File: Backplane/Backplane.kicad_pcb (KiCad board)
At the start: 2 copper layers, 245 parts, among them J3 Bus_PCI_Express_x1, J4 Bus_PCI_Express_x1, J5 Bus_PCI_Express_x1, J6 Bus_PCI_Express_x1, Q1 CJ2302 S2, Q12 CJ2302 S2, Q13 CJ2302 S2, Q14 CJ2302 S2, Q15 CJ2302 S2, Q16 CJ2302 S2, Q17 CJ2302 S2, Q18 CJ2302 S2, Q19 CJ2302 S2, Q2 CJ2302 S2, Q20 CJ2302 S2, Q21 CJ2302 S2, Q22 CJ2302 S2, Q23 CJ2302 S2, Q24 CJ2302 S2, Q25 CJ2302 S2, Q26 CJ2302 S2, Q27 CJ2302 S2, Q28 CJ2302 S2, Q3 TPHR8504PL,LQ(M1W, Q4 TPHR8504PL,LQ(M1W, Q5 TPHR8504PL,LQ(M1W, Q6 TPHR8504PL,LQ(M1W, Q7 CJ2302 S2, U1 XT60PW-F_C428722, U10 XT60PW-F_C428722, U11 PCA9555PW,118, U12 LM393, U13 LM358, U14 TCA9548APWR, U15 MCP4725A0T-E/CH, U16 MCP4725A0T-E/CH, U2 XT60PW-F_C428722, U22 ADS1115IDGSR, U24 ADS1115IDGSR, U3 LM393, U31 PCA9555PW,118, U32 TCA9548APWR, U33 LM393, U34 UCC27324DR, U35 LM358, U36 MCP4725A0T-E/CH, U37 MCP4725A0T-E/CH, U38 ADS1115IDGSR, U39 ADS1115IDGSR, U4 LM358, U5 TPS54360BDDAR, U6 TPS54360BDDAR, U7 TPS54360BDDAR, U8 UCC27324DR, U9 XT60PW-F_C428722

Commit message: Finished board layout.
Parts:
- moved J3 353.0 mm to (88.5, 203.2)
- moved R24 307.8 mm to (670.1, 97.5)
- moved R25 307.8 mm to (670.1, 100.7)
- moved R26 307.8 mm to (670.1, 104.0)
- moved R27 307.8 mm to (670.1, 107.3)
- moved R28 307.8 mm to (670.1, 110.6)
- moved U12 307.8 mm to (670.8, 91.7)
- moved U13 307.8 mm to (677.1, 91.7)
- moved U3 307.8 mm to (658.3, 91.7)
- moved U4 307.8 mm to (664.6, 91.7)
- moved Q3 307.8 mm to (677.1, 100.7)
- moved Q4 307.8 mm to (684.5, 100.7)
- moved R16 307.8 mm to (664.1, 97.5)
- moved R17 307.8 mm to (664.1, 100.7)
- moved R18 307.8 mm to (664.1, 104.0)
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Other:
- board outline added: 520 x 80 mm

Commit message: All parts are correct.
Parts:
- removed C10, C11, C12, C13, C14, C15, C16, C4, C5: 100n, Resistor_SMD:R_1206_3216Metric_Pad1.30x1.75mm_HandSolder
- removed D32, D33, D34, D35: S5BBF, COMPONENTS:SMBF_L4.3-W3.6-LS5.3-RD
- removed L4: FXL1040-8R2-M, COMPONENTS:IND-SMD_L11.5-W10.0_FXL1040
- removed Q16, Q17, Q23, Q24: CJ2302 S2, COMPONENTS:SOT-23-3_L3.0-W1.7-P0.95-LS2.9-BR
- removed R34, R35, R36, R37, R39, R40, R41, R42, R43, R44, R45, R46, R47, R69, R70, R71, R72, R73, R74, R75, R76, R77, R78, R79, R80, R81, R82: 1k, Resistor_SMD:R_1206_3216Metric_Pad1.30x1.75mm_HandSolder
- removed R38: 8k, Resistor_SMD:R_1206_3216Metric_Pad1.30x1.75mm_HandSolder
- removed U11, U31: PCA9555PW,118, COMPONENTS:TSSOP-24_L7.8-W4.4-P0.65-LS6.4-BL
- removed U12, U3: LM393, COMPONENTS:SOP-8_L4.9-W3.9-P1.27-LS6.0-BL
- removed U13, U4: LM358, COMPONENTS:SOP-8_L4.9-W3.9-P1.27-LS6.0-BL
- removed U14: TCA9548APWR, COMPONENTS:TSSOP-24_L7.8-W4.4-P0.65-LS6.4-BL
- removed U24: ADS1115IDGSR, COMPONENTS:MSOP-10_L3.0-W3.0-P0.50-LS5.0-BL
- removed U36, U37: MCP4725A0T-E/CH, COMPONENTS:SOT-23-6_L2.9-W1.6-P0.95-LS2.8-BL
- removed U5, U6: TPS54360BDDAR, COMPONENTS:SOIC-8_L5.0-W4.0-P1.27-LS6.0-BL-EP2.0
- added C49: 100n, Resistor_SMD:R_1206_3216Metric_Pad1.30x1.75mm_HandSolder, F.Cu at (292.4, 207.6)
- added C50: 100n, Resistor_SMD:R_1206_3216Metric_Pad1.30x1.75mm_HandSolder, F.Cu at (298.3, 191.1)
- added C51: 100n, Resistor_SMD:R_1206_3216Metric_Pad1.30x1.75mm_HandSolder, F.Cu at (298.3, 194.4)
- added C52: 100n, Resistor_SMD:R_1206_3216Metric_Pad1.30x1.75mm_HandSolder, F.Cu at (-106.7, 527.5)
- added C53: 100n, Resistor_SMD:R_1206_3216Metric_Pad1.30x1.75mm_HandSolder, F.Cu at (-106.7, 530.8)
- added C54: 100n, Resistor_SMD:R_1206_3216Metric_Pad1.30x1.75mm_HandSolder, F.Cu at (-106.7, 534.0)
- added C55: 100n, Resistor_SMD:R_1206_3216Metric_Pad1.30x1.75mm_HandSolder, F.Cu at (-106.7, 537.3)
- added C56: 100n, Resistor_SMD:R_1206_3216Metric_Pad1.30x1.75mm_HandSolder, F.Cu at (-106.7, 540.6)
- added C57: 100n, Resistor_SMD:R_1206_3216Metric_Pad1.30x1.75mm_HandSolder, F.Cu at (-106.7, 543.9)
- added C58: 100n, Resistor_SMD:R_1206_3216Metric_Pad1.30x1.75mm_HandSolder, F.Cu at (-106.7, 547.2)
- added C59: 100n, Resistor_SMD:R_1206_3216Metric_Pad1.30x1.75mm_HandSolder, F.Cu at (-106.4, 464.1)
- added C60: 100n, Resistor_SMD:R_1206_3216Metric_Pad1.30x1.75mm_HandSolder, F.Cu at (-106.4, 467.4)
- added C61: 100n, Resistor_SMD:R_1206_3216Metric_Pad1.30x1.75mm_HandSolder, F.Cu at (-106.4, 470.7)
- added C62: 100n, Resistor_SMD:R_1206_3216Metric_Pad1.30x1.75mm_HandSolder, F.Cu at (-106.4, 474.0)
- added C63: 100n, Resistor_SMD:R_1206_3216Metric_Pad1.30x1.75mm_HandSolder, F.Cu at (-106.4, 477.3)
- added C64: 100n, Resistor_SMD:R_1206_3216Metric_Pad1.30x1.75mm_HandSolder, F.Cu at (-106.4, 480.6)
- added C65: 100n, Resistor_SMD:R_1206_3216Metric_Pad1.30x1.75mm_HandSolder, F.Cu at (-106.4, 483.9)
- added D24: LED, LED_SMD:LED_1206_3216Metric, F.Cu at (657.9, -215.7)
- added D25: LED, LED_SMD:LED_1206_3216Metric, F.Cu at (657.9, -212.3)
- added D26: LED, LED_SMD:LED_1206_3216Metric, F.Cu at (657.9, -208.9)
- added D27: LED, LED_SMD:LED_1206_3216Metric, F.Cu at (657.9, -205.5)
- added H1: MountingHole_Pad, MountingHole:MountingHole_3.2mm_M3_Pad_TopBottom, F.Cu at (45.2, 170.0)
- added H2: MountingHole_Pad, MountingHole:MountingHole_3.2mm_M3_Pad_TopBottom, F.Cu at (545.0, 230.0)
- added H3: MountingHole_Pad, MountingHole:MountingHole_3.2mm_M3_Pad_TopBottom, F.Cu at (545.3, 170.0)
- added H4: MountingHole_Pad, MountingHole:MountingHole_3.2mm_M3_Pad_TopBottom, F.Cu at (355.0, 230.0)
- added H5: MountingHole_Pad, MountingHole:MountingHole_3.2mm_M3_Pad_TopBottom, F.Cu at (229.9, 230.0)
- added H6: MountingHole_Pad, MountingHole:MountingHole_3.2mm_M3_Pad_TopBottom, F.Cu at (45.0, 230.0)
- added H7: MountingHole_Pad, MountingHole:MountingHole_3.2mm_M3_Pad_TopBottom, F.Cu at (355.2, 170.0)
- added H8: MountingHole_Pad, MountingHole:MountingHole_3.2mm_M3_Pad_TopBottom, F.Cu at (230.0, 170.0)
- added L1: FXL1040-8R2-M, COMPONENTS:IND-SMD_L11.5-W10.0_FXL1040, F.Cu at (222.0, 442.7)
- added Q10: CJ2302 S2, COMPONENTS:SOT-23-3_L3.0-W1.7-P0.95-LS2.9-BR, F.Cu at (645.1, -140.5)
- added Q11: CJ2302 S2, COMPONENTS:SOT-23-3_L3.0-W1.7-P0.95-LS2.9-BR, F.Cu at (640.0, -79.9)
- added Q8: CJ2302 S2, COMPONENTS:SOT-23-3_L3.0-W1.7-P0.95-LS2.9-BR, F.Cu at (645.1, -149.0)
- added Q9: CJ2302 S2, COMPONENTS:SOT-23-3_L3.0-W1.7-P0.95-LS2.9-BR, F.Cu at (645.1, -144.7)
- added R113: 0, Resistor_SMD:R_1206_3216Metric_Pad1.30x1.75mm_HandSolder, F.Cu at (410.2, 197.2)
- added R114: 1k, Resistor_SMD:R_1206_3216Metric_Pad1.30x1.75mm_HandSolder, F.Cu at (298.3, 197.7)
- added R115: 1k, Resistor_SMD:R_1206_3216Metric_Pad1.30x1.75mm_HandSolder, F.Cu at (298.3, 201.0)
- added R116: 1k, Resistor_SMD:R_1206_3216Metric_Pad1.30x1.75mm_HandSolder, F.Cu at (298.3, 204.3)
- added R117: 1k, Resistor_SMD:R_1206_3216Metric_Pad1.30x1.75mm_HandSolder, F.Cu at (298.3, 207.6)
- added R118: 1k, Resistor_SMD:R_1206_3216Metric_Pad1.30x1.75mm_HandSolder, F.Cu at (304.3, 191.1)
- added R119: 1k, Resistor_SMD:R_1206_3216Metric_Pad1.30x1.75mm_HandSolder, F.Cu at (304.3, 194.4)
- added R120: 1k, Resistor_SMD:R_1206_3216Metric_Pad1.30x1.75mm_HandSolder, F.Cu at (304.3, 197.7)
- added R121: 1k, Resistor_SMD:R_1206_3216Metric_Pad1.30x1.75mm_HandSolder, F.Cu at (304.3, 201.0)
- added R122: 10k, Resistor_SMD:R_1206_3216Metric_Pad1.30x1.75mm_HandSolder, F.Cu at (-106.7, 550.5)
- added R123: 10k, Resistor_SMD:R_1206_3216Metric_Pad1.30x1.75mm_HandSolder, F.Cu at (-100.7, 527.5)
- added R124: 1k, Resistor_SMD:R_1206_3216Metric_Pad1.30x1.75mm_HandSolder, F.Cu at (-100.7, 530.8)
- added R125: 1k, Resistor_SMD:R_1206_3216Metric_Pad1.30x1.75mm_HandSolder, F.Cu at (-100.7, 534.0)
- added R126: 1k, Resistor_SMD:R_1206_3216Metric_Pad1.30x1.75mm_HandSolder, F.Cu at (-100.7, 537.3)
- added R127: 1k, Resistor_SMD:R_1206_3216Metric_Pad1.30x1.75mm_HandSolder, F.Cu at (-100.7, 540.6)
- added R128: 1k, Resistor_SMD:R_1206_3216Metric_Pad1.30x1.75mm_HandSolder, F.Cu at (-100.7, 543.9)
- added R129: 1k, Resistor_SMD:R_1206_3216Metric_Pad1.30x1.75mm_HandSolder, F.Cu at (-100.7, 547.2)
- added R130: 100k, Resistor_SMD:R_1206_3216Metric_Pad1.30x1.75mm_HandSolder, F.Cu at (-100.7, 550.5)
- added R131: 100k, Resistor_SMD:R_1206_3216Metric_Pad1.30x1.75mm_HandSolder, F.Cu at (-94.8, 527.5)
- added R132: 1k, Resistor_SMD:R_1206_3216Metric_Pad1.30x1.75mm_HandSolder, F.Cu at (-94.8, 530.8)
- added R133: 1k, Resistor_SMD:R_1206_3216Metric_Pad1.30x1.75mm_HandSolder, F.Cu at (-94.8, 534.0)
- added R134: 0.003, Resistor_SMD:R_1206_3216Metric_Pad1.30x1.75mm_HandSolder, F.Cu at (-94.8, 537.3)
- added R135: 0.003, Resistor_SMD:R_1206_3216Metric_Pad1.30x1.75mm_HandSolder, F.Cu at (-94.8, 540.6)
- added R136: 10k, Resistor_SMD:R_1206_3216Metric_Pad1.30x1.75mm_HandSolder, F.Cu at (-106.4, 487.2)
- added R137: 10k, Resistor_SMD:R_1206_3216Metric_Pad1.30x1.75mm_HandSolder, F.Cu at (-100.4, 464.1)
- added R138: 1k, Resistor_SMD:R_1206_3216Metric_Pad1.30x1.75mm_HandSolder, F.Cu at (-100.4, 467.4)
- added R139: 1k, Resistor_SMD:R_1206_3216Metric_Pad1.30x1.75mm_HandSolder, F.Cu at (-100.4, 470.7)
- added R140: 1k, Resistor_SMD:R_1206_3216Metric_Pad1.30x1.75mm_HandSolder, F.Cu at (-100.4, 474.0)
- added R141: 1k, Resistor_SMD:R_1206_3216Metric_Pad1.30x1.75mm_HandSolder, F.Cu at (-100.4, 477.3)
- added R142: 1k, Resistor_SMD:R_1206_3216Metric_Pad1.30x1.75mm_HandSolder, F.Cu at (-100.4, 480.6)
- added R143: 1k, Resistor_SMD:R_1206_3216Metric_Pad1.30x1.75mm_HandSolder, F.Cu at (-100.4, 483.9)
- added R144: 100k, Resistor_SMD:R_1206_3216Metric_Pad1.30x1.75mm_HandSolder, F.Cu at (-100.4, 487.2)
- added R145: 100k, Resistor_SMD:R_1206_3216Metric_Pad1.30x1.75mm_HandSolder, F.Cu at (-94.5, 464.1)
- added R146: 1k, Resistor_SMD:R_1206_3216Metric_Pad1.30x1.75mm_HandSolder, F.Cu at (-94.5, 467.4)
- added R147: 1k, Resistor_SMD:R_1206_3216Metric_Pad1.30x1.75mm_HandSolder, F.Cu at (-94.5, 470.7)
- added R148: 0.003, Resistor_SMD:R_1206_3216Metric_Pad1.30x1.75mm_HandSolder, F.Cu at (-94.5, 474.0)
- added R149: 0.003, Resistor_SMD:R_1206_3216Metric_Pad1.30x1.75mm_HandSolder, F.Cu at (-94.5, 477.3)
- added U17: ADS1115IDGSR, COMPONENTS:MSOP-10_L3.0-W3.0-P0.50-LS5.0-BL, F.Cu at (-187.5, 381.6)
- added U18: TCA9548APWR, COMPONENTS:TSSOP-24_L7.8-W4.4-P0.65-LS6.4-BL, F.Cu at (442.1, -461.8)
- added U19: ADS1115IDGSR, COMPONENTS:MSOP-10_L3.0-W3.0-P0.50-LS5.0-BL, F.Cu at (-180.9, 381.6)
- added U20: PCA9555PW,118, COMPONENTS:TSSOP-24_L7.8-W4.4-P0.65-LS6.4-BL, F.Cu at (-184.9, 371.9)
- added U21: TPS54360BDDAR, COMPONENTS:SOIC-8_L5.0-W4.0-P1.27-LS6.0-BL-EP2.0, F.Cu at (232.7, 441.4)
- added U23: TPS54360BDDAR, COMPONENTS:SOIC-8_L5.0-W4.0-P1.27-LS6.0-BL-EP2.0, F.Cu at (219.6, 547.8)
- added U28: LM393, COMPONENTS:SOP-8_L4.9-W3.9-P1.27-LS6.0-BL, F.Cu at (-84.1, 546.0)
- added U29: UCC27324DR, COMPONENTS:SOIC-8_L5.0-W4.0-P1.27-LS6.0-BL, F.Cu at (-83.4, 537.7)
- C23, C24, C25, C26, C27, C28: value 100n -> 2.2u; footprint Resistor_SMD:R_1206_3216Metric_Pad1.30x1.75mm_HandSolder -> Capacitor_SMD:C_1206_3216Metric
- C29: value 2.2u -> 0.1u
- C31: value 6800p -> 0.1u
- C32: value 39p -> 6800p
- C33, C34: value 47u -> 6800p
- C35, C36: value 2.2u -> 39p
- C37: value 0.1u -> 39p
- C38: value 6800p -> 47u
- C39: value 39p -> 47u
- C42, C43: value 2.2u -> 47u
- C44: value 0.1u -> 100n; footprint Capacitor_SMD:C_1206_3216Metric -> Resistor_SMD:R_1206_3216Metric_Pad1.30x1.75mm_HandSolder
- C45: value 6800p -> 100n; footprint Capacitor_SMD:C_1206_3216Metric -> Resistor_SMD:R_1206_3216Metric_Pad1.30x1.75mm_HandSolder
- C46: value 39p -> 100n; footprint Capacitor_SMD:C_1206_3216Metric -> Resistor_SMD:R_1206_3216Metric_Pad1.30x1.75mm_HandSolder
- C47, C48: value 47u -> 100n; footprint Capacitor_SMD:C_1206_3216Metric -> Resistor_SMD:R_1206_3216Metric_Pad1.30x1.75mm_HandSolder
- C8: value 2.2u -> 100n; footprint Capacitor_SMD:C_1206_3216Metric -> Resistor_SMD:R_1206_3216Metric_Pad1.30x1.75mm_HandSolder
- D1, D2, D3, D4, D5, D6, D7, D8: value LED -> S5BBF; footprint LED_SMD:LED_1206_3216Metric -> COMPONENTS:SMBF_L4.3-W3.6-LS5.3-RD
- D21, D22, D23: value B560C-13-F -> LED; footprint COMPONENTS:SMC_L7.1-W6.2-LS8.1-RD -> LED_SMD:LED_1206_3216Metric
- D28: value S5BBF -> LED; footprint COMPONENTS:SMBF_L4.3-W3.6-LS5.3-RD -> LED_SMD:LED_1206_3216Metric
- D29, D30, D31: value S5BBF -> B560C-13-F; footprint COMPONENTS:SMBF_L4.3-W3.6-LS5.3-RD -> COMPONENTS:SMC_L7.1-W6.2-LS8.1-RD
- Q25, Q26, Q27, Q28: value CJ2302 S2 -> TPHR8504PL,LQ(M1W; footprint COMPONENTS:SOT-23-3_L3.0-W1.7-P0.95-LS2.9-BR -> COMPONENTS:DFN-5_L4.9-W5.9-P1.27-LS6.2-BL
- Q3, Q4, Q5, Q6: value TPHR8504PL,LQ(M1W -> CJ2302 S2; footprint COMPONENTS:DFN-5_L4.9-W5.9-P1.27-LS6.2-BL -> COMPONENTS:SOT-23-3_L3.0-W1.7-P0.95-LS2.9-BR
- R1, R2, R3: moved to B.Cu
- R10: value 300k -> 1k
- R100, R99: value 1k -> 162k
- R101: value 100k -> 162k
- R102: value 100k -> 13k
- R103, R104: value 1k -> 13k
- R105: value 0.003 -> 53.6k
- R106: value 0.003 -> 140k
- R107: value 13k -> 300k
- R108: value 140k -> 3k
- R109: value 0 -> 2k
- R11, R7: value 10.2k -> 1k
- R110, R112: value 0 -> 10.2k
- R12: value 3k -> 1k
- R13: value 2k -> 1k
- R14, R8: value 162k -> 1k
- R15, R16, R29, R94: value 10k -> 1k
- R22, R26, R32: value 1k -> 8k
- R23, R24: value 100k -> 1k
- R27: value 0.003 -> 1k
- R28: value 0.003 -> 8k
- R30, R31, R90: value 8k -> 1k
- R4: value 162k -> 0
- R5: value 13k -> 0
- R6: value 53.6k -> 0
- R9: value 13k -> 1k
- U15, U16: value MCP4725A0T-E/CH -> ADS1115IDGSR; footprint COMPONENTS:SOT-23-6_L2.9-W1.6-P0.95-LS2.8-BL -> COMPONENTS:MSOP-10_L3.0-W3.0-P0.50-LS5.0-BL
- U22: value ADS1115IDGSR -> TPS54360BDDAR; footprint COMPONENTS:MSOP-10_L3.0-W3.0-P0.50-LS5.0-BL -> COMPONENTS:SOIC-8_L5.0-W4.0-P1.27-LS6.0-BL-EP2.0
- U32: value TCA9548APWR -> MCP4725A0T-E/CH; footprint COMPONENTS:TSSOP-24_L7.8-W4.4-P0.65-LS6.4-BL -> COMPONENTS:SOT-23-6_L2.9-W1.6-P0.95-LS2.8-BL
- U33: value LM393 -> MCP4725A0T-E/CH; footprint COMPONENTS:SOP-8_L4.9-W3.9-P1.27-LS6.0-BL -> COMPONENTS:SOT-23-6_L2.9-W1.6-P0.95-LS2.8-BL
- U34: value UCC27324DR -> LM393; footprint COMPONENTS:SOIC-8_L5.0-W4.0-P1.27-LS6.0-BL -> COMPONENTS:SOP-8_L4.9-W3.9-P1.27-LS6.0-BL
- U35: value LM358 -> UCC27324DR; footprint COMPONENTS:SOP-8_L4.9-W3.9-P1.27-LS6.0-BL -> COMPONENTS:SOIC-8_L5.0-W4.0-P1.27-LS6.0-BL
- U38, U39: value ADS1115IDGSR -> MCP4725A0T-E/CH; footprint COMPONENTS:MSOP-10_L3.0-W3.0-P0.50-LS5.0-BL -> COMPONENTS:SOT-23-6_L2.9-W1.6-P0.95-LS2.8-BL
- U7: value TPS54360BDDAR -> PCA9555PW,118; footprint COMPONENTS:SOIC-8_L5.0-W4.0-P1.27-LS6.0-BL-EP2.0 -> COMPONENTS:TSSOP-24_L7.8-W4.4-P0.65-LS6.4-BL
- U8: value UCC27324DR -> TCA9548APWR; footprint COMPONENTS:SOIC-8_L5.0-W4.0-P1.27-LS6.0-BL -> COMPONENTS:TSSOP-24_L7.8-W4.4-P0.65-LS6.4-BL
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- renumbered J5 to J1, J6 to J2, J4 to J3, J3 to J4
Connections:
- C17 pad 1: +3.3V -> +5V
- C18 pad 1: +3.3V -> +5V
- C19 pad 1: +3.3V -> +5V
- C20 pad 1: GND -> +3.3V
- C20 pad 2: Net-(U37-VOUT) -> GND
- C21 pad 1: +3V3 -> +5V
- C22 pad 1: +5V -> +3.3V
- C23 pad 1: +3V3 -> +BATT
- C24 pad 1: +5V -> +BATT
- C25 pad 1: +5V -> +48V
- C26 pad 1: +5V -> +BATT
- C27 pad 1: +12V -> +BATT
- C28 pad 1: +12V -> +48V
- C29 pad 1: +BATT -> Net-(U21-BOOT)
- C29 pad 2: GND -> Net-(D29-K)
- C30 pad 1: Net-(U5-BOOT) -> Net-(U22-BOOT)
- C30 pad 2: Net-(D21-K) -> Net-(D30-K)
- C31 pad 1: Net-(C31-Pad1) -> Net-(U23-BOOT)
- C31 pad 2: GND -> Net-(D31-K)
- C32 pad 1: Net-(U5-COMP) -> Net-(C32-Pad1)
- C33 pad 1: +5V -> Net-(C33-Pad1)
- C34 pad 1: +5V -> Net-(C34-Pad1)
- C35 pad 1: +48V -> Net-(U21-COMP)
- C36 pad 1: +48V -> Net-(U22-COMP)
- C37 pad 1: Net-(U6-BOOT) -> Net-(U23-COMP)
- C37 pad 2: Net-(D22-K) -> GND
- C38 pad 1: Net-(C38-Pad1) -> +5V
- C39 pad 1: Net-(U6-COMP) -> +12V
- C41 pad 1: +24V -> +5V
- C42 pad 1: +BATT -> +12V
- C43 pad 1: +BATT -> +24V
- C44 pad 1: Net-(U7-BOOT) -> GNDPWR
- C44 pad 2: Net-(D23-K) -> GND
- C45 pad 1: Net-(C45-Pad1) -> GNDPWR
- C46 pad 1: Net-(U7-COMP) -> GNDPWR
- C47 pad 1: +12V -> GNDPWR
- C48 pad 1: +12V -> GNDPWR
- C8 pad 1: +BATT -> +3.3V
- C9 pad 1: GND -> +3.3V
- C9 pad 2: Net-(U15-VOUT) -> GND
- D1 pad 1: Net-(D1-K) -> /BatPair1/BatMax - Female/P+
- D1 pad 2: +5V -> +24V
- D2 pad 1: Net-(D2-K) -> /BatPair2/BatMax - Female/P+
- D2 pad 2: +5V -> +24V
- D21 pad 2: GND -> +5V
- D22 pad 2: GND -> +5V
- D23 pad 2: GND -> +5V
- D28 pad 1: /BatPair1/BatMax - Female1/P+ -> Net-(D28-K)
- D28 pad 2: +24V -> +5V
- D29 pad 1: /BatPair1/BatMax - Female/P+ -> Net-(D29-K)
- D29 pad 2: +24V -> GND
- D3 pad 1: Net-(D3-K) -> +BATT
- D3 pad 2: +5V -> /BatPair2/BatMax - Female/P+
- D30 pad 1: /BatPair2/BatMax - Female/P+ -> Net-(D30-K)
- D30 pad 2: +24V -> GND
- D31 pad 1: /BatPair2/BatMax - Female1/P+ -> Net-(D31-K)
- D31 pad 2: +24V -> GND
- D4 pad 1: Net-(D4-K) -> +BATT
- D4 pad 2: +5V -> /BatPair1/BatMax - Female/P+
- D5 pad 1: Net-(D5-K) -> +BATT
- D5 pad 2: +5V -> /BatPair2/BatMax - Female1/P+
- D6 pad 1: Net-(D6-K) -> +BATT
- D6 pad 2: +5V -> /BatPair1/BatMax - Female1/P+
- D7 pad 1: Net-(D7-K) -> /BatPair1/BatMax - Female1/P+
- D7 pad 2: +5V -> +24V
- D8 pad 1: Net-(D8-K) -> /BatPair2/BatMax - Female1/P+
- D8 pad 2: +5V -> +24V
- FPC1 pad 30: unconnected-(FPC1-Pad30) -> /PSUS/EN_BAT_CHG_VLT
- J1 pad A10: /BatPair2/BatMax - Female/P- -> /BatPair1/BatMax - Female1/P-
- J1 pad A11: /BatPair2/BatMax - Female/P- -> /BatPair1/BatMax - Female1/P-
- J1 pad A12: /BatPair2/BatMax - Female/P- -> /BatPair1/BatMax - Female1/P-
- J1 pad A13: /BatPair2/BatMax - Female/P- -> /BatPair1/BatMax - Female1/P-
- J1 pad A14: /BatPair2/BatMax - Female/P- -> /BatPair1/BatMax - Female1/P-
- J1 pad A15: /BatPair2/BatMax - Female/P- -> /BatPair1/BatMax - Female1/P-
- J1 pad A16: /BatPair2/BatMax - Female/P- -> /BatPair1/BatMax - Female1/P-
- J1 pad A17: /BatPair2/BatMax - Female/P- -> /BatPair1/BatMax - Female1/P-
- J1 pad A18: /BatPair2/BatMax - Female/P- -> /BatPair1/BatMax - Female1/P-
- J1 pad A2: /BatPair2/BatMax - Female/SCL -> /BatPair1/BatMax - Female1/SCL
- J1 pad A3: /BatPair2/BatMax - Female/TEMP -> /BatPair1/BatMax - Female1/TEMP
- J1 pad A6: /BatPair2/BatMax - Female/P- -> /BatPair1/BatMax - Female1/P-
- J1 pad A7: /BatPair2/BatMax - Female/P- -> /BatPair1/BatMax - Female1/P-
- J1 pad A8: /BatPair2/BatMax - Female/P- -> /BatPair1/BatMax - Female1/P-
- J1 pad A9: /BatPair2/BatMax - Female/P- -> /BatPair1/BatMax - Female1/P-
- J1 pad B10: /BatPair2/BatMax - Female/P+ -> /BatPair1/BatMax - Female1/P+
- J1 pad B11: /BatPair2/BatMax - Female/P+ -> /BatPair1/BatMax - Female1/P+
- J1 pad B12: /BatPair2/BatMax - Female/P+ -> /BatPair1/BatMax - Female1/P+
- J1 pad B13: /BatPair2/BatMax - Female/P+ -> /BatPair1/BatMax - Female1/P+
- J1 pad B14: /BatPair2/BatMax - Female/P+ -> /BatPair1/BatMax - Female1/P+
- J1 pad B15: /BatPair2/BatMax - Female/P+ -> /BatPair1/BatMax - Female1/P+
- J1 pad B16: /BatPair2/BatMax - Female/P+ -> /BatPair1/BatMax - Female1/P+
- J1 pad B17: /BatPair2/BatMax - Female/P+ -> /BatPair1/BatMax - Female1/P+
- J1 pad B18: /BatPair2/BatMax - Female/P+ -> /BatPair1/BatMax - Female1/P+
- J1 pad B2: /BatPair2/BatMax - Female/SDA -> /BatPair1/BatMax - Female1/SDA
- J1 pad B3: /BatPair2/BatMax - Female/EEPROM_WC -> /BatPair1/BatMax - Female1/EEPROM_WC
- J1 pad B6: /BatPair2/BatMax - Female/P+ -> /BatPair1/BatMax - Female1/P+
- J1 pad B7: /BatPair2/BatMax - Female/P+ -> /BatPair1/BatMax - Female1/P+
- J1 pad B8: /BatPair2/BatMax - Female/P+ -> /BatPair1/BatMax - Female1/P+
- J1 pad B9: /BatPair2/BatMax - Female/P+ -> /BatPair1/BatMax - Female1/P+
- J2 pad A10: /BatPair2/BatMax - Female1/P- -> /BatPair1/BatMax - Female/P-
- J2 pad A11: /BatPair2/BatMax - Female1/P- -> /BatPair1/BatMax - Female/P-
- J2 pad A12: /BatPair2/BatMax - Female1/P- -> /BatPair1/BatMax - Female/P-
- J2 pad A13: /BatPair2/BatMax - Female1/P- -> /BatPair1/BatMax - Female/P-
- J2 pad A14: /BatPair2/BatMax - Female1/P- -> /BatPair1/BatMax - Female/P-
- J2 pad A15: /BatPair2/BatMax - Female1/P- -> /BatPair1/BatMax - Female/P-
- J2 pad A16: /BatPair2/BatMax - Female1/P- -> /BatPair1/BatMax - Female/P-
- J2 pad A17: /BatPair2/BatMax - Female1/P- -> /BatPair1/BatMax - Female/P-
- J2 pad A18: /BatPair2/BatMax - Female1/P- -> /BatPair1/BatMax - Female/P-
- J2 pad A2: /BatPair2/BatMax - Female1/SCL -> /BatPair1/BatMax - Female/SCL
- J2 pad A3: /BatPair2/BatMax - Female1/TEMP -> /BatPair1/BatMax - Female/TEMP
- J2 pad A6: /BatPair2/BatMax - Female1/P- -> /BatPair1/BatMax - Female/P-
- J2 pad A7: /BatPair2/BatMax - Female1/P- -> /BatPair1/BatMax - Female/P-
- J2 pad A8: /BatPair2/BatMax - Female1/P- -> /BatPair1/BatMax - Female/P-
- J2 pad A9: /BatPair2/BatMax - Female1/P- -> /BatPair1/BatMax - Female/P-
- J2 pad B10: /BatPair2/BatMax - Female1/P+ -> /BatPair1/BatMax - Female/P+
- J2 pad B11: /BatPair2/BatMax - Female1/P+ -> /BatPair1/BatMax - Female/P+
- J2 pad B12: /BatPair2/BatMax - Female1/P+ -> /BatPair1/BatMax - Female/P+
- J2 pad B13: /BatPair2/BatMax - Female1/P+ -> /BatPair1/BatMax - Female/P+
- J2 pad B14: /BatPair2/BatMax - Female1/P+ -> /BatPair1/BatMax - Female/P+
- J2 pad B15: /BatPair2/BatMax - Female1/P+ -> /BatPair1/BatMax - Female/P+
- J2 pad B16: /BatPair2/BatMax - Female1/P+ -> /BatPair1/BatMax - Female/P+
- J2 pad B17: /BatPair2/BatMax - Female1/P+ -> /BatPair1/BatMax - Female/P+
- J2 pad B18: /BatPair2/BatMax - Female1/P+ -> /BatPair1/BatMax - Female/P+
- J2 pad B2: /BatPair2/BatMax - Female1/SDA -> /BatPair1/BatMax - Female/SDA
- J2 pad B3: /BatPair2/BatMax - Female1/EEPROM_WC -> /BatPair1/BatMax - Female/EEPROM_WC
- J2 pad B6: /BatPair2/BatMax - Female1/P+ -> /BatPair1/BatMax - Female/P+
- J2 pad B7: /BatPair2/BatMax - Female1/P+ -> /BatPair1/BatMax - Female/P+
- J2 pad B8: /BatPair2/BatMax - Female1/P+ -> /BatPair1/BatMax - Female/P+
- J2 pad B9: /BatPair2/BatMax - Female1/P+ -> /BatPair1/BatMax - Female/P+
- J3 pad A10: /BatPair1/BatMax - Female1/P- -> /BatPair2/BatMax - Female/P-
- J3 pad A11: /BatPair1/BatMax - Female1/P- -> /BatPair2/BatMax - Female/P-
- J3 pad A12: /BatPair1/BatMax - Female1/P- -> /BatPair2/BatMax - Female/P-
- J3 pad A13: /BatPair1/BatMax - Female1/P- -> /BatPair2/BatMax - Female/P-
- J3 pad A14: /BatPair1/BatMax - Female1/P- -> /BatPair2/BatMax - Female/P-
- J3 pad A15: /BatPair1/BatMax - Female1/P- -> /BatPair2/BatMax - Female/P-
- J3 pad A16: /BatPair1/BatMax - Female1/P- -> /BatPair2/BatMax - Female/P-
- J3 pad A17: /BatPair1/BatMax - Female1/P- -> /BatPair2/BatMax - Female/P-
- J3 pad A18: /BatPair1/BatMax - Female1/P- -> /BatPair2/BatMax - Female/P-
- J3 pad A2: /BatPair1/BatMax - Female1/SCL -> /BatPair2/BatMax - Female/SCL
- J3 pad A3: /BatPair1/BatMax - Female1/TEMP -> /BatPair2/BatMax - Female/TEMP
- J3 pad A6: /BatPair1/BatMax - Female1/P- -> /BatPair2/BatMax - Female/P-
- J3 pad A7: /BatPair1/BatMax - Female1/P- -> /BatPair2/BatMax - Female/P-
- J3 pad A8: /BatPair1/BatMax - Female1/P- -> /BatPair2/BatMax - Female/P-
- J3 pad A9: /BatPair1/BatMax - Female1/P- -> /BatPair2/BatMax - Female/P-
- J3 pad B10: /BatPair1/BatMax - Female1/P+ -> /BatPair2/BatMax - Female/P+
- J3 pad B11: /BatPair1/BatMax - Female1/P+ -> /BatPair2/BatMax - Female/P+
- J3 pad B12: /BatPair1/BatMax - Female1/P+ -> /BatPair2/BatMax - Female/P+
- J3 pad B13: /BatPair1/BatMax - Female1/P+ -> /BatPair2/BatMax - Female/P+
- J3 pad B14: /BatPair1/BatMax - Female1/P+ -> /BatPair2/BatMax - Female/P+
- J3 pad B15: /BatPair1/BatMax - Female1/P+ -> /BatPair2/BatMax - Female/P+
- J3 pad B16: /BatPair1/BatMax - Female1/P+ -> /BatPair2/BatMax - Female/P+
- J3 pad B17: /BatPair1/BatMax - Female1/P+ -> /BatPair2/BatMax - Female/P+
- J3 pad B18: /BatPair1/BatMax - Female1/P+ -> /BatPair2/BatMax - Female/P+
- J3 pad B2: /BatPair1/BatMax - Female1/SDA -> /BatPair2/BatMax - Female/SDA
- J3 pad B3: /BatPair1/BatMax - Female1/EEPROM_WC -> /BatPair2/BatMax - Female/EEPROM_WC
- J3 pad B6: /BatPair1/BatMax - Female1/P+ -> /BatPair2/BatMax - Female/P+
- J3 pad B7: /BatPair1/BatMax - Female1/P+ -> /BatPair2/BatMax - Female/P+
- J3 pad B8: /BatPair1/BatMax - Female1/P+ -> /BatPair2/BatMax - Female/P+
- J3 pad B9: /BatPair1/BatMax - Female1/P+ -> /BatPair2/BatMax - Female/P+
- J4 pad A10: /BatPair1/BatMax - Female/P- -> /BatPair2/BatMax - Female1/P-
- J4 pad A11: /BatPair1/BatMax - Female/P- -> /BatPair2/BatMax - Female1/P-
- J4 pad A12: /BatPair1/BatMax - Female/P- -> /BatPair2/BatMax - Female1/P-
- J4 pad A13: /BatPair1/BatMax - Female/P- -> /BatPair2/BatMax - Female1/P-
- J4 pad A14: /BatPair1/BatMax - Female/P- -> /BatPair2/BatMax - Female1/P-
- J4 pad A15: /BatPair1/BatMax - Female/P- -> /BatPair2/BatMax - Female1/P-
- J4 pad A16: /BatPair1/BatMax - Female/P- -> /BatPair2/BatMax - Female1/P-
- J4 pad A17: /BatPair1/BatMax - Female/P- -> /BatPair2/BatMax - Female1/P-
- J4 pad A18: /BatPair1/BatMax - Female/P- -> /BatPair2/BatMax - Female1/P-
- J4 pad A2: /BatPair1/BatMax - Female/SCL -> /BatPair2/BatMax - Female1/SCL
- J4 pad A3: /BatPair1/BatMax - Female/TEMP -> /BatPair2/BatMax - Female1/TEMP
- J4 pad A6: /BatPair1/BatMax - Female/P- -> /BatPair2/BatMax - Female1/P-
- J4 pad A7: /BatPair1/BatMax - Female/P- -> /BatPair2/BatMax - Female1/P-
- J4 pad A8: /BatPair1/BatMax - Female/P- -> /BatPair2/BatMax - Female1/P-
- J4 pad A9: /BatPair1/BatMax - Female/P- -> /BatPair2/BatMax - Female1/P-
- J4 pad B10: /BatPair1/BatMax - Female/P+ -> /BatPair2/BatMax - Female1/P+
- J4 pad B11: /BatPair1/BatMax - Female/P+ -> /BatPair2/BatMax - Female1/P+
- J4 pad B12: /BatPair1/BatMax - Female/P+ -> /BatPair2/BatMax - Female1/P+
- J4 pad B13: /BatPair1/BatMax - Female/P+ -> /BatPair2/BatMax - Female1/P+
- J4 pad B14: /BatPair1/BatMax - Female/P+ -> /BatPair2/BatMax - Female1/P+
- J4 pad B15: /BatPair1/BatMax - Female/P+ -> /BatPair2/BatMax - Female1/P+
- J4 pad B16: /BatPair1/BatMax - Female/P+ -> /BatPair2/BatMax - Female1/P+
- J4 pad B17: /BatPair1/BatMax - Female/P+ -> /BatPair2/BatMax - Female1/P+
- J4 pad B18: /BatPair1/BatMax - Female/P+ -> /BatPair2/BatMax - Female1/P+
- J4 pad B2: /BatPair1/BatMax - Female/SDA -> /BatPair2/BatMax - Female1/SDA
- J4 pad B3: /BatPair1/BatMax - Female/EEPROM_WC -> /BatPair2/BatMax - Female1/EEPROM_WC
- J4 pad B6: /BatPair1/BatMax - Female/P+ -> /BatPair2/BatMax - Female1/P+
- J4 pad B7: /BatPair1/BatMax - Female/P+ -> /BatPair2/BatMax - Female1/P+
- J4 pad B8: /BatPair1/BatMax - Female/P+ -> /BatPair2/BatMax - Female1/P+
- J4 pad B9: /BatPair1/BatMax - Female/P+ -> /BatPair2/BatMax - Female1/P+
- L2 pad 1: Net-(D21-K) -> Net-(D30-K)
- L2 pad 2: +5V -> +12V
- L3 pad 1: Net-(D22-K) -> Net-(D31-K)
- Q12 pad 1: /BAT_LEDS/LED1 -> /BAT_LEDS3/LED2
- Q13 pad 1: /BAT_LEDS1/LED2 -> /BAT_LEDS3/LED3
- Q14 pad 1: /BAT_LEDS2/LED2 -> /BAT_LEDS3/LED4
- Q15 pad 1: /BAT_LEDS2/LED2 -> /BAT_LEDS3/LED5
- Q18 pad 1: /BAT_LEDS2/LED3 -> /BAT_LEDS4/LED1
- Q19 pad 1: /BAT_LEDS2/LED3 -> /BAT_LEDS4/LED2
- Q2 pad 1: /BAT_LEDS2/LED1 -> /BAT_LEDS1/LED2
- Q20 pad 1: /BAT_LEDS/LED3 -> /BAT_LEDS4/LED3
- Q21 pad 1: /BAT_LEDS1/LED4 -> /BAT_LEDS4/LED4
- Q22 pad 1: /BAT_LEDS2/LED4 -> /BAT_LEDS4/LED5
- Q25 pad 1: /BAT_LEDS1/LED5 -> Net-(U3A-+)
- Q25 pad 2: GND -> Net-(U3A-+)
- Q25 pad 3: Net-(Q25-D) -> Net-(U3A-+)
- Q26 pad 1: /BAT_LEDS2/LED5 -> Net-(U3B-+)
- Q26 pad 2: GND -> Net-(U3B-+)
- Q26 pad 3: Net-(Q26-D) -> Net-(U3B-+)
- Q27 pad 1: /BAT_LEDS2/LED5 -> Net-(U4A-+)
- Q27 pad 2: GND -> Net-(U4A-+)
- Q27 pad 3: Net-(Q27-D) -> Net-(U4A-+)
- Q28 pad 1: /BAT_LEDS/LED5 -> Net-(U4B-+)
- Q28 pad 2: GND -> Net-(U4B-+)
- Q28 pad 3: Net-(Q28-D) -> Net-(U4B-+)
- Q3 pad 1: Net-(U13A-+) -> /BAT_LEDS1/LED3
- Q3 pad 2: Net-(U13A-+) -> GND
- Q3 pad 3: Net-(U13A-+) -> Net-(Q3-D)
- Q4 pad 1: Net-(U4B-+) -> /BAT_LEDS1/LED4
- Q4 pad 2: Net-(U4B-+) -> GND
- Q4 pad 3: Net-(U4B-+) -> Net-(Q4-D)
- Q5 pad 1: Net-(U35A-+) -> /BAT_LEDS1/LED5
- Q5 pad 2: Net-(U35A-+) -> GND
- Q5 pad 3: Net-(U35A-+) -> Net-(Q5-D)
- Q6 pad 1: Net-(U13B-+) -> /BAT_LEDS2/LED1
- Q6 pad 2: Net-(U13B-+) -> GND
- Q6 pad 3: Net-(U13B-+) -> Net-(Q6-D)
- Q7 pad 1: /BAT_LEDS2/LED1 -> /BAT_LEDS2/LED2
- R10 pad 1: +24V -> Net-(D12-K)
- R10 pad 2: Net-(R10-Pad2) -> Net-(Q4-D)
- R100 pad 1: /BatPair2/ADS1118/A2 -> Net-(U22-RT/CLK)
- R100 pad 2: Net-(R100-Pad2) -> GND
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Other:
- copper layers 2 -> 6

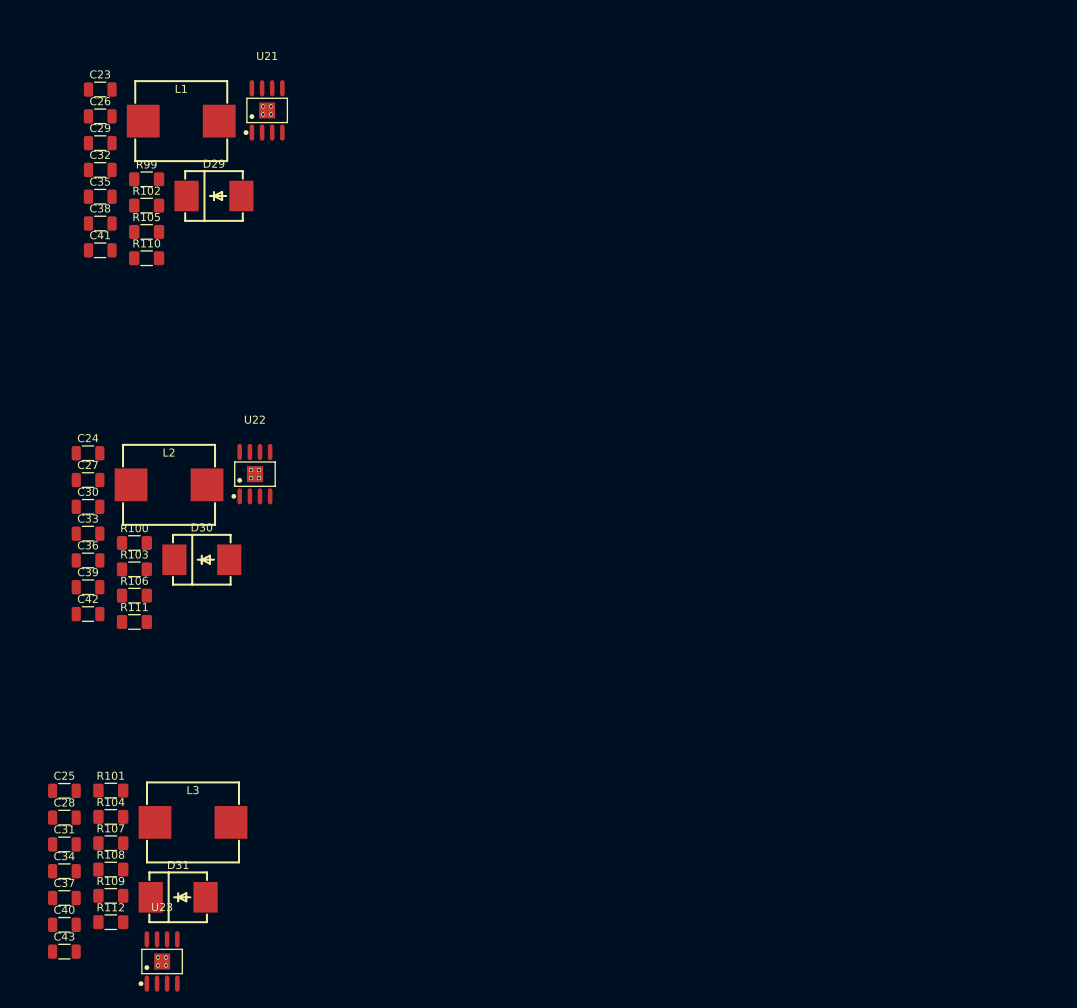
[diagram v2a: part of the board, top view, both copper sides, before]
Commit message: Power supplies are layed out.
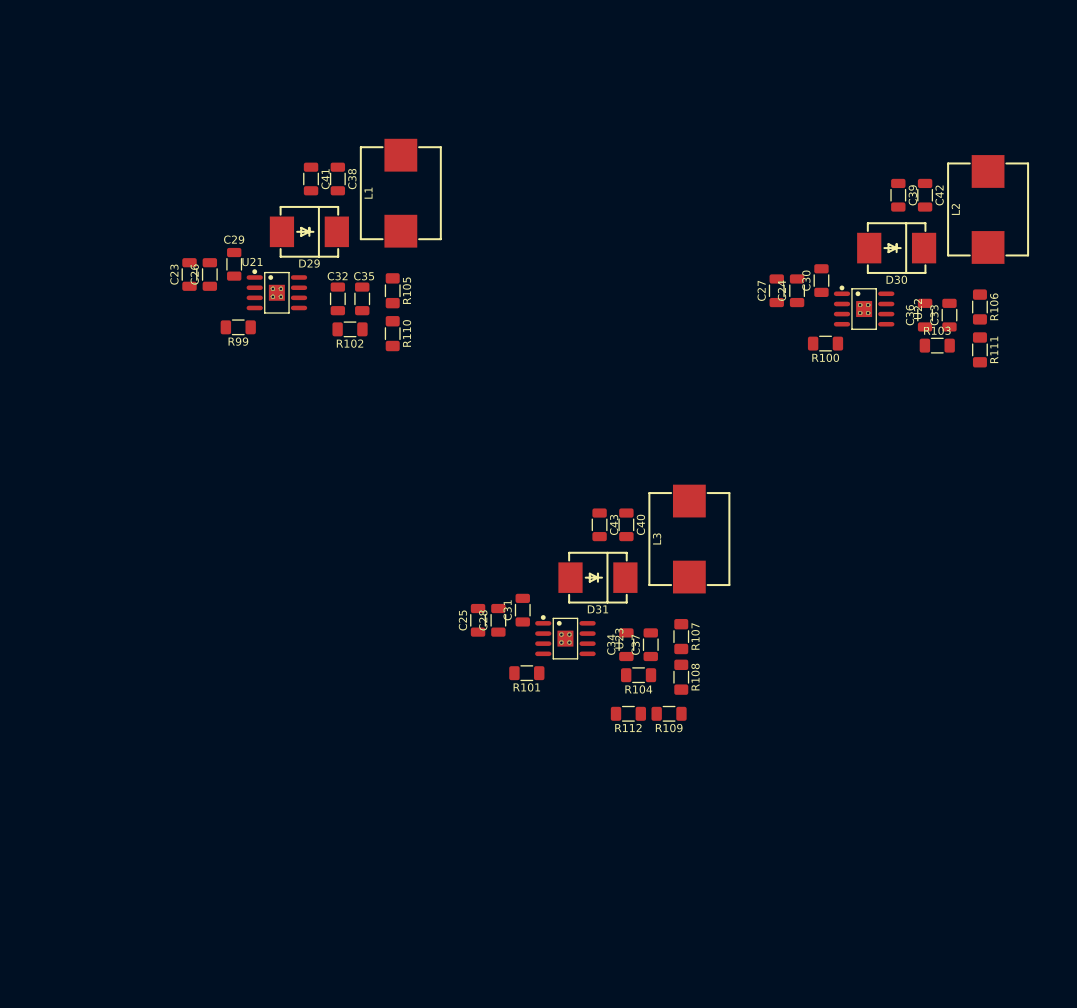
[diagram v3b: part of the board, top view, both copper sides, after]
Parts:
- moved C42 117.0 mm to (315.0, 452.0), turned to -90 degrees
- moved C39 112.5 mm to (311.6, 452.0), turned to -90 degrees
- moved R106 111.7 mm to (321.8, 465.9), turned to -90 degrees
- moved C33 111.1 mm to (318.0, 467.0), turned to 90 degrees
- moved R111 111.0 mm to (321.8, 471.3), turned to -90 degrees
- moved C36 109.0 mm to (315.0, 467.0), turned to 90 degrees
- moved L2 108.0 mm to (322.9, 453.7), turned to 90 degrees
- moved R103 104.2 mm to (316.5, 470.8)
- moved C30 95.9 mm to (302.0, 462.6), turned to 90 degrees
- moved D30 95.2 mm to (311.4, 458.6), turned to 180 degrees
- moved C24 90.9 mm to (299.0, 463.9), turned to 90 degrees
- moved R100 89.9 mm to (302.5, 470.5), turned to 180 degrees
- moved C27 89.3 mm to (296.4, 463.9), turned to 90 degrees
- moved C40 86.2 mm to (277.6, 493.2), turned to -90 degrees
- moved C43 85.6 mm to (274.3, 493.2), turned to -90 degrees
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
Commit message: Done with first I2CMux Layout.
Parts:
- R53, R54, R55, R56, R57, R58, R59, R60, R61, R62, R63, R64, R65, R66, R67, R68: moved to B.Cu
- moved R4 523.6 mm to (287.3, -57.0)
- moved R5 523.6 mm to (299.0, -57.6)
- moved R6 523.6 mm to (305.3, -61.6)
- moved C21 447.5 mm to (-178.6, 386.9)
- moved R31 295.3 mm to (482.6, 215.5)
- moved R32 295.3 mm to (482.6, 218.8)
- moved R33 295.3 mm to (482.6, 222.1)
- moved R63 33.1 mm to (459.5, -510.9), turned to 180 degrees
- moved R61 33.1 mm to (459.5, -506.4), turned to 180 degrees
- moved R62 32.6 mm to (459.5, -508.7), turned to 180 degrees
- moved R68 30.1 mm to (459.5, -522.4), turned to 180 degrees
- moved C9 28.7 mm to (449.6, -520.9), turned to 180 degrees
- moved R64 28.0 mm to (459.5, -513.2), turned to 180 degrees
- moved R67 28.0 mm to (459.5, -520.1), turned to 180 degrees
- moved R65 26.8 mm to (459.5, -515.5), turned to 180 degrees
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
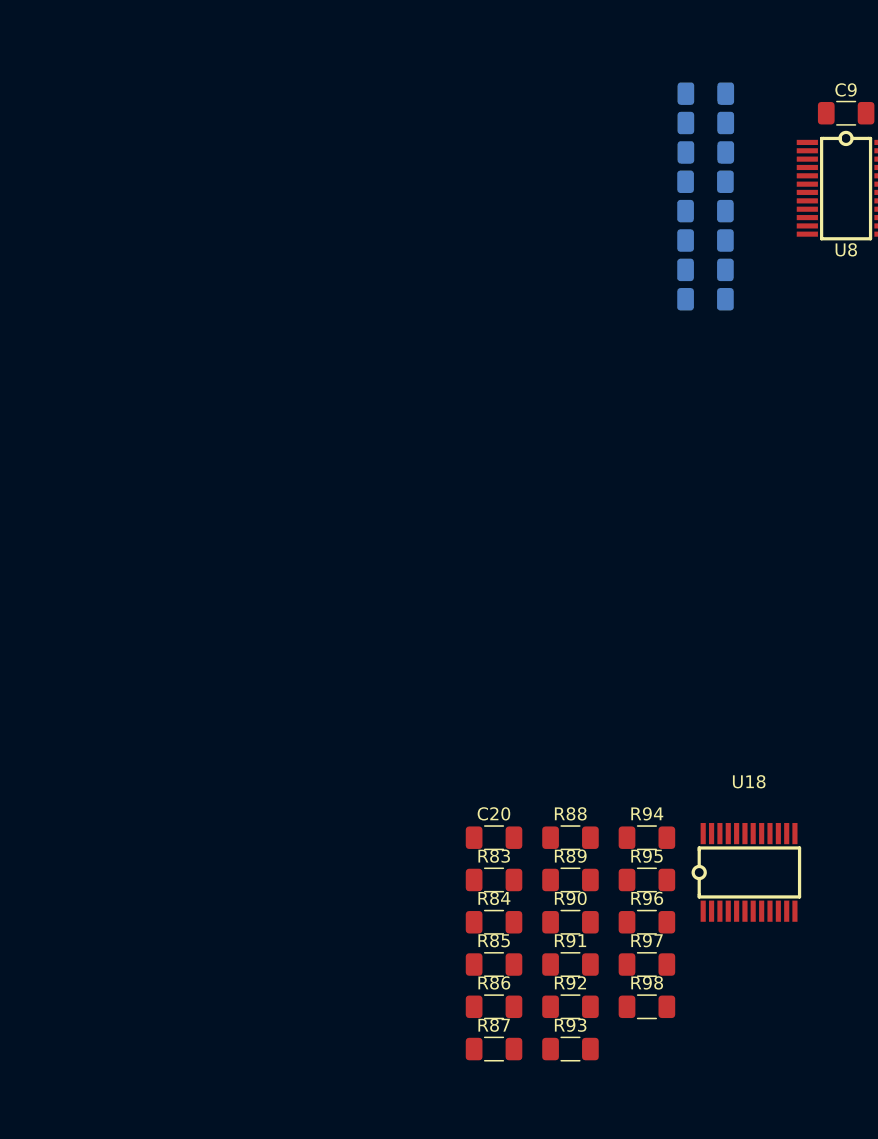
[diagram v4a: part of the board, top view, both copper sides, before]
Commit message: Finished with second I2C layout.
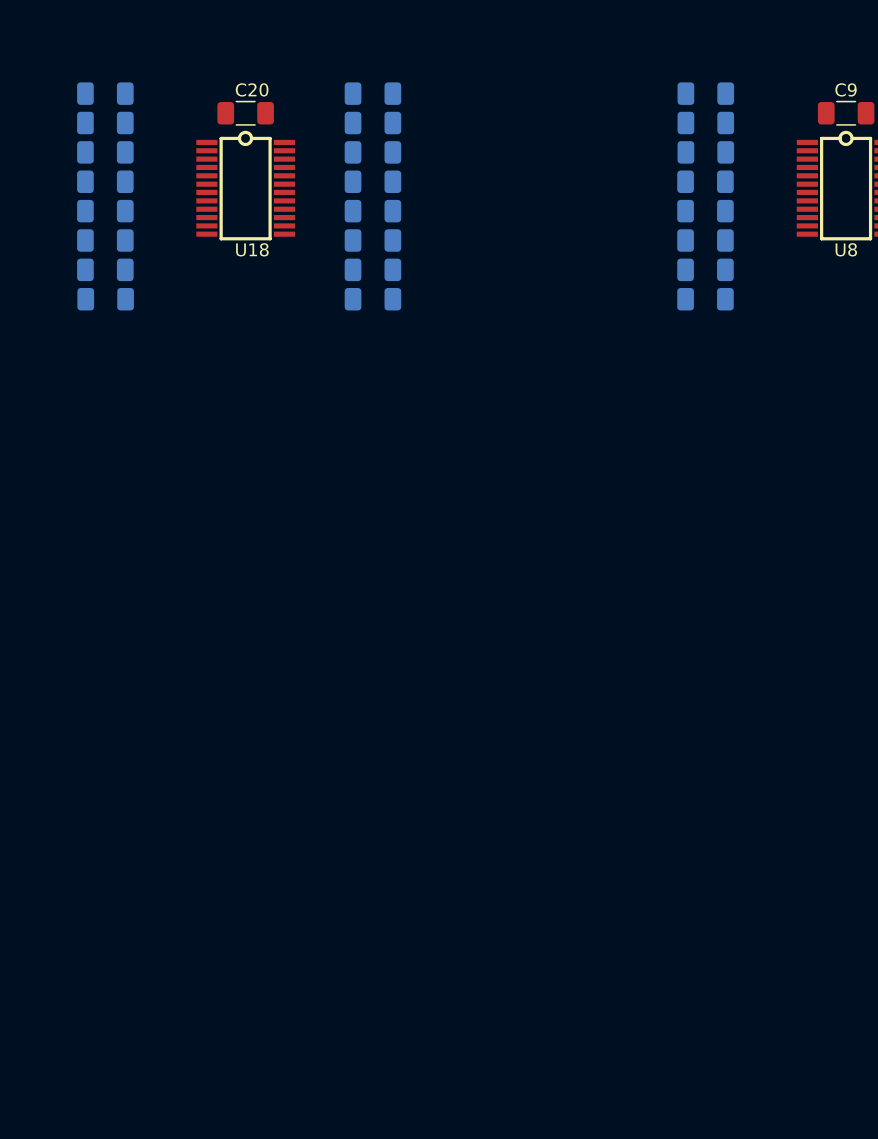
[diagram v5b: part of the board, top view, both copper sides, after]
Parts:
- R83, R84, R85, R86, R87, R88, R89, R90, R91, R92, R93, R94, R95, R96, R97, R98: moved to B.Cu
- moved R98 74.2 mm to (412.8, -522.4), turned to 180 degrees
- moved R87 71.9 mm to (391.9, -513.2)
- moved R86 71.0 mm to (391.9, -515.5)
- moved R85 70.1 mm to (391.9, -517.8)
- moved R84 69.2 mm to (391.9, -520.1)
- moved R97 68.9 mm to (412.8, -520.1), turned to 180 degrees
- moved R83 68.3 mm to (391.9, -522.4)
- moved U18 66.1 mm to (402.9, -515.0), turned to -90 degrees
- moved R93 64.8 mm to (412.8, -510.9), turned to 180 degrees
- moved R96 63.6 mm to (412.8, -517.8), turned to 180 degrees
- moved R90 60.5 mm to (392.0, -506.4)
- moved R89 59.7 mm to (391.9, -508.7)
- moved C20 59.6 mm to (402.9, -520.9), turned to 180 degrees
- moved R92 59.4 mm to (412.8, -508.7), turned to 180 degrees
- moved R88 58.9 mm to (391.9, -510.9)
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
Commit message: EarthGround Done.
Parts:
- C44, C45, C46, C47, C48, C49, C50, C51, R114, R115, R116, R117, R118, R119, R120, R121: moved to B.Cu
- moved R120 254.4 mm to (52.1, 231.0)
- moved R118 253.4 mm to (51.9, 169.0)
- moved C45 247.4 mm to (538.5, 168.8), turned to 180 degrees
- moved C48 247.4 mm to (538.5, 229.5), turned to 180 degrees
- moved C46 242.3 mm to (52.1, 228.7)
- moved R115 242.0 mm to (538.5, 171.0), turned to 180 degrees
- moved R116 241.8 mm to (538.5, 231.7), turned to 180 degrees
- moved C44 241.3 mm to (51.9, 171.3)
- moved R119 84.6 mm to (223.5, 169.3), turned to 180 degrees
- moved C47 74.9 mm to (223.5, 171.6), turned to 180 degrees
- moved C50 74.0 mm to (361.9, 229.0)
- moved C51 70.8 mm to (236.5, 229.0)
- moved R114 70.3 mm to (236.5, 231.2)
- moved C49 68.7 mm to (348.3, 167.7), turned to 180 degrees
- moved R121 65.1 mm to (361.9, 231.2)
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
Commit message: First LED Bank Done.
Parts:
- moved R52 401.1 mm to (424.2, 119.2), turned to 180 degrees
- moved R51 399.7 mm to (424.2, 114.1), turned to 180 degrees
- moved R50 398.3 mm to (424.2, 109.1), turned to 180 degrees
- moved R49 396.8 mm to (424.2, 104.0), turned to 180 degrees
- moved R48 395.4 mm to (424.2, 98.9), turned to 180 degrees
- moved Q22 394.4 mm to (419.2, 119.2), turned to 180 degrees
- moved D28 394.4 mm to (429.3, 119.2)
- moved Q21 393.7 mm to (419.2, 114.1), turned to 180 degrees
- moved Q20 393.0 mm to (419.2, 109.1), turned to 180 degrees
- moved D27 393.0 mm to (429.3, 114.1)
- moved Q19 392.3 mm to (419.2, 104.0), turned to 180 degrees
- moved Q18 391.6 mm to (419.2, 98.9), turned to 180 degrees
- moved D26 391.6 mm to (429.3, 109.1)
- moved D25 390.3 mm to (429.3, 104.0)
- moved D24 388.9 mm to (429.3, 98.9)

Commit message: Done with layout for first current control
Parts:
- added U3: LM358, COMPONENTS:SOP-8_L4.9-W3.9-P1.27-LS6.0-BL, B.Cu at (151.2, 176.1)
- added U4: LM358, COMPONENTS:SOP-8_L4.9-W3.9-P1.27-LS6.0-BL, F.Cu at (157.4, 280.4)
- C52, C53, C54, C55, C56, C57, Q25, Q26, R122, R123, R124, R125, R126, R127, R128, R129, R130, R131, R132, R133, R134, R135, U28, U29, U32, U33: moved to B.Cu
- moved C21 712.7 mm to (334.0, -108.3)
- moved U17 712.7 mm to (325.1, -113.6)
- moved U19 712.7 mm to (331.6, -113.6)
- moved U20 712.7 mm to (327.7, -123.3)
- moved C20 683.5 mm to (207.0, 134.0)
- moved R83 683.5 mm to (196.1, 132.4)
- moved R84 683.5 mm to (196.1, 134.7)
- moved R85 683.5 mm to (196.1, 137.0)
- moved R86 683.5 mm to (196.1, 139.3)
- moved R87 683.5 mm to (196.1, 141.6)
- moved R88 683.5 mm to (196.1, 143.9)
- moved R89 683.5 mm to (196.1, 146.2)
- moved R90 683.5 mm to (196.1, 148.4)
- moved R91 683.5 mm to (216.9, 148.4)
- moved R92 683.5 mm to (216.9, 146.2)
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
